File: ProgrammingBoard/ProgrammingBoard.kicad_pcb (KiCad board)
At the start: 4 copper layers, 34 x 69.5 mm, 6 parts, among them J1 X0511WVS-24AS-LPV01, J2 X0511FVS-24AS-LPV01, J3 X0511WVS-24AS-LPV01, J4 X0511FVS-24AS-LPV01, J5 Conn_01x20, J6 Conn_01x20

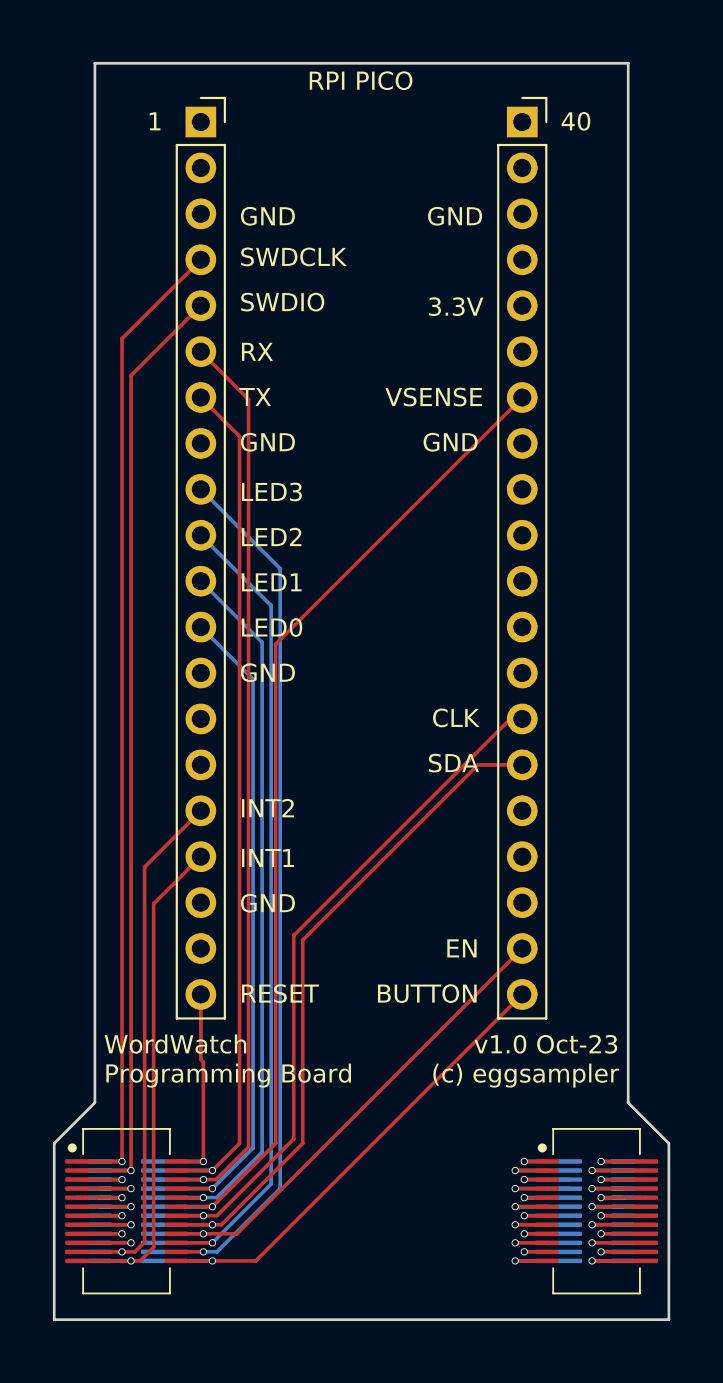
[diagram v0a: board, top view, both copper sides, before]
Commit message: Remove LED driver
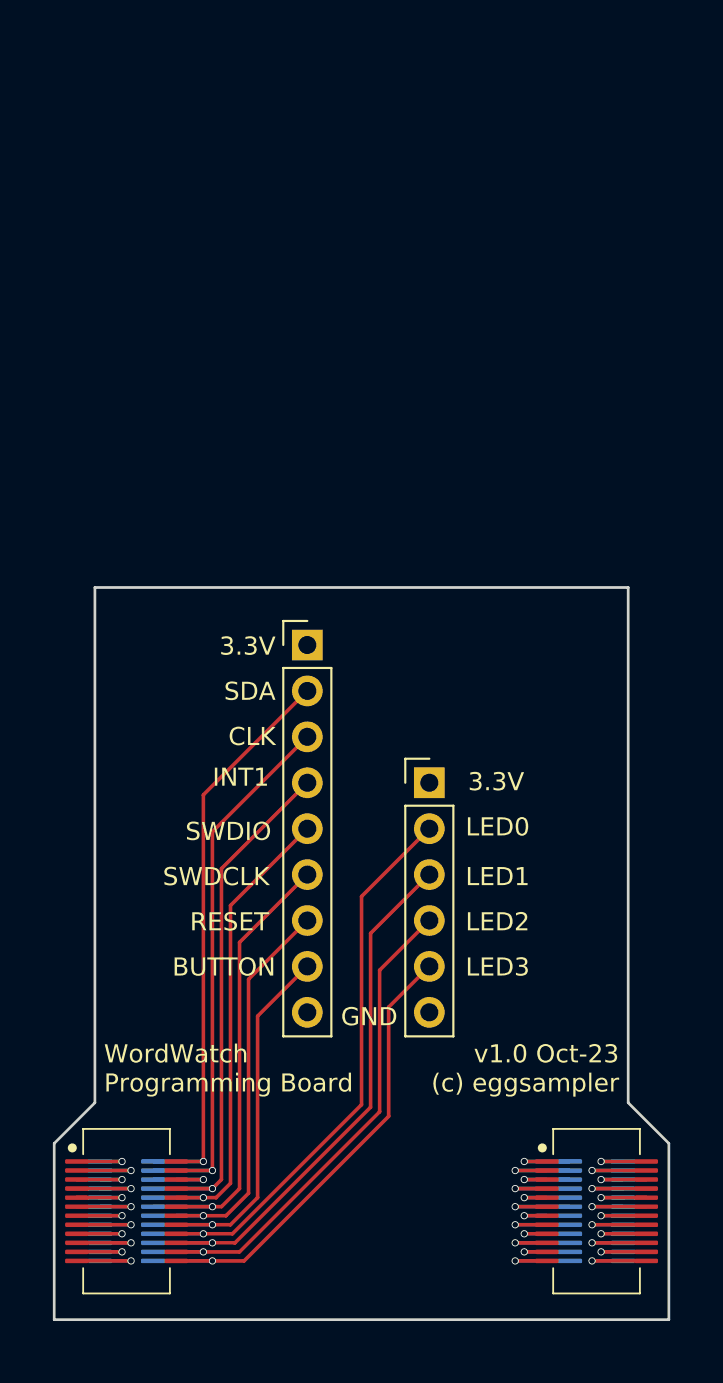
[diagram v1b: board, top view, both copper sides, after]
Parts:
- J5: value Conn_01x20 -> Conn_01x06; footprint Connector_PinSocket_2.54mm:PinSocket_1x20_P2.54mm_Vertical -> Connector_PinHeader_2.54mm:PinHeader_1x06_P2.54mm_Vertical
- J6: value Conn_01x20 -> Conn_01x09; footprint Connector_PinSocket_2.54mm:PinSocket_1x20_P2.54mm_Vertical -> Connector_PinHeader_2.54mm:PinHeader_1x09_P2.54mm_Vertical
- moved J5 38.7 mm to (130.8, 72.8)
- moved J6 31.3 mm to (124.0, 65.2)
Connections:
- J3 pad 1: /Connectors/RESET -> /Connectors/SDA
- J3 pad 11: /Connectors/VSENSE -> /Connectors/SWDCLK
- J3 pad 13: /Connectors/SCL -> /Connectors/RESET
- J3 pad 15: /Connectors/SDA -> /Connectors/BUTTON
- J3 pad 17: /Connectors/LED_EN -> /Connectors/LED0
- J3 pad 19: /Connectors/LED2 -> /Connectors/LED1
- J3 pad 2: /Connectors/SWDCLK -> VCC
- J3 pad 21: /Connectors/LED3 -> /Connectors/LED2
- J3 pad 22: /Connectors/INT2 -> GND
- J3 pad 23: /Connectors/BUTTON -> /Connectors/LED3
- J3 pad 24: /Connectors/INT1 -> GND
- J3 pad 3: /Connectors/TX -> /Connectors/SCL
- J3 pad 4: /Connectors/SWDIO -> VCC
- J3 pad 5: /Connectors/RX -> GND
- J3 pad 7: /Connectors/LED0 -> /Connectors/INT1
- J3 pad 9: /Connectors/LED1 -> /Connectors/SWDIO
- J4 pad 1: /Connectors/SWDCLK -> VCC
- J4 pad 10: /Connectors/LED1 -> /Connectors/SWDIO
- J4 pad 12: /Connectors/VSENSE -> /Connectors/SWDCLK
- J4 pad 14: /Connectors/SCL -> /Connectors/RESET
- J4 pad 16: /Connectors/SDA -> /Connectors/BUTTON
- J4 pad 18: /Connectors/LED_EN -> /Connectors/LED0
- J4 pad 2: /Connectors/RESET -> /Connectors/SDA
- J4 pad 20: /Connectors/LED2 -> /Connectors/LED1
- J4 pad 21: /Connectors/INT2 -> GND
- J4 pad 22: /Connectors/LED3 -> /Connectors/LED2
- J4 pad 23: /Connectors/INT1 -> GND
- J4 pad 24: /Connectors/BUTTON -> /Connectors/LED3
- J4 pad 3: /Connectors/SWDIO -> VCC
- J4 pad 4: /Connectors/TX -> /Connectors/SCL
- J4 pad 6: /Connectors/RX -> GND
- J4 pad 8: /Connectors/LED0 -> /Connectors/INT1
- J5 pad 1: unconnected-(J5-Pin_1-Pad1) -> VCC
- J5 pad 2: unconnected-(J5-Pin_2-Pad2) -> /Connectors/LED0
- J5 pad 3: GND -> /Connectors/LED1
- J5 pad 4: /Connectors/SWDCLK -> /Connectors/LED2
- J5 pad 5: /Connectors/SWDIO -> /Connectors/LED3
- J5 pad 6: /Connectors/RX -> GND
- J6 pad 1: unconnected-(J6-Pin_1-Pad1) -> VCC
- J6 pad 2: unconnected-(J6-Pin_2-Pad2) -> /Connectors/SDA
- J6 pad 3: GND -> /Connectors/SCL
- J6 pad 4: unconnected-(J6-Pin_4-Pad4) -> /Connectors/INT1
- J6 pad 5: VCC -> /Connectors/SWDIO
- J6 pad 6: unconnected-(J6-Pin_6-Pad6) -> /Connectors/SWDCLK
- J6 pad 7: /Connectors/VSENSE -> /Connectors/RESET
- J6 pad 8: GND -> /Connectors/BUTTON
- J6 pad 9: unconnected-(J6-Pin_9-Pad9) -> GND
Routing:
- net /Connectors/VSENSE: track 57.1 -> 0.00 mm, vias 1 -> 0
- net /Connectors/RX: track 52.6 -> 0.00 mm, vias 1 -> 0
- net /Connectors/TX: track 49.5 -> 0.00 mm, vias 1 -> 0
- net /Connectors/INT2: track 30.3 -> 0.00 mm, vias 1 -> 0
- net /Connectors/SWDCLK: track 55.4 -> 26.1 mm
- net /Connectors/LED_EN: track 28.5 -> 0.00 mm, vias 1 -> 0
- net /Connectors/SWDIO: track 54.2 -> 27.5 mm
- net /Connectors/LED3: track 50.5 -> 27.6 mm
- net /Connectors/LED2: track 47.4 -> 29.0 mm
- net GND: track 29.1 -> 41.8 mm, vias 7 -> 10
- net /Connectors/LED1: track 41.6 -> 31.3 mm
- net /Connectors/RESET: track 13.6 -> 23.7 mm
- net VCC: track 16.9 -> 25.3 mm, vias 4 -> 6
- net /Connectors/SCL: track 39.9 -> 31.4 mm
- net /Connectors/SDA: track 39.5 -> 32.7 mm
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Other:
- board size 34 x 69.5 mm -> 34 x 40.5 mm
- board text removed: "1"
- board text removed: "40"
- board text removed: "EN"
- board text removed: "INT2"
- board text removed: "RPI PICO"
- board text removed: "RX"
- board text removed: "TX"
- board text removed: "VSENSE"

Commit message: Change led matrix routing for sinking current through mcu, sourcing from battery
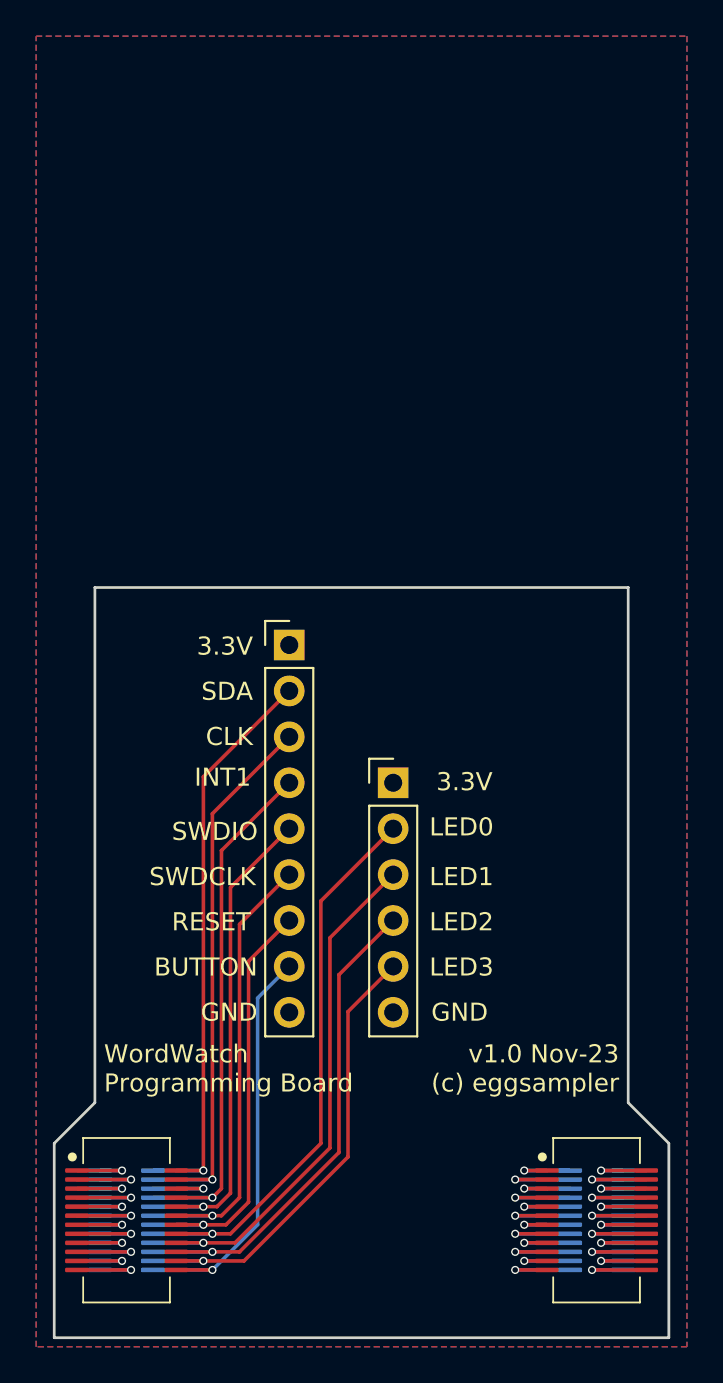
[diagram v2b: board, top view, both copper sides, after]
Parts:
- moved J5 2.00 mm to (128.8, 72.8)
- moved J6 1.00 mm to (123.0, 65.2)
- moved J1 0.50 mm to (140.0, 97.0)
- moved J2 0.50 mm to (140.0, 97.0)
- moved J3 0.50 mm to (114.0, 97.0)
- moved J4 0.50 mm to (114.0, 97.0)
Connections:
- J1 pad 10: /Connectors/COL1 -> /Connectors/ROW3
- J1 pad 11: /Connectors/ROW4 -> /Connectors/COL4
- J1 pad 12: /Connectors/COL2 -> /Connectors/ROW4
- J1 pad 13: /Connectors/ROW5 -> /Connectors/COL5
- J1 pad 14: /Connectors/COL3 -> /Connectors/ROW5
- J1 pad 15: /Connectors/ROW6 -> /Connectors/COL6
- J1 pad 16: /Connectors/COL4 -> /Connectors/ROW6
- J1 pad 17: /Connectors/ROW7 -> /Connectors/COL7
- J1 pad 18: /Connectors/COL5 -> /Connectors/ROW7
- J1 pad 19: /Connectors/ROW8 -> /Connectors/COL8
- J1 pad 20: /Connectors/COL6 -> /Connectors/ROW8
- J1 pad 21: /Connectors/ROW9 -> /Connectors/COL9
- J1 pad 22: /Connectors/COL7 -> /Connectors/ROW9
- J1 pad 23: GND -> /Connectors/COL10
- J1 pad 24: /Connectors/COL8 -> GND
- J1 pad 3: /Connectors/ROW0 -> /Connectors/COL0
- J1 pad 4: /Connectors/COL9 -> /Connectors/ROW0
- J1 pad 5: /Connectors/ROW1 -> /Connectors/COL1
- J1 pad 6: /Connectors/COL10 -> /Connectors/ROW1
- J1 pad 7: /Connectors/ROW2 -> /Connectors/COL2
- J1 pad 8: /Connectors/COL0 -> /Connectors/ROW2
- J1 pad 9: /Connectors/ROW3 -> /Connectors/COL3
- J2 pad 10: /Connectors/ROW3 -> /Connectors/COL3
- J2 pad 11: /Connectors/COL2 -> /Connectors/ROW4
- J2 pad 12: /Connectors/ROW4 -> /Connectors/COL4
- J2 pad 13: /Connectors/COL3 -> /Connectors/ROW5
- J2 pad 14: /Connectors/ROW5 -> /Connectors/COL5
- J2 pad 15: /Connectors/COL4 -> /Connectors/ROW6
- J2 pad 16: /Connectors/ROW6 -> /Connectors/COL6
- J2 pad 17: /Connectors/COL5 -> /Connectors/ROW7
- J2 pad 18: /Connectors/ROW7 -> /Connectors/COL7
- J2 pad 19: /Connectors/COL6 -> /Connectors/ROW8
- J2 pad 20: /Connectors/ROW8 -> /Connectors/COL8
- J2 pad 21: /Connectors/COL7 -> /Connectors/ROW9
- J2 pad 22: /Connectors/ROW9 -> /Connectors/COL9
- J2 pad 23: /Connectors/COL8 -> GND
- J2 pad 24: GND -> /Connectors/COL10
- J2 pad 3: /Connectors/COL9 -> /Connectors/ROW0
- J2 pad 4: /Connectors/ROW0 -> /Connectors/COL0
- J2 pad 5: /Connectors/COL10 -> /Connectors/ROW1
- J2 pad 6: /Connectors/ROW1 -> /Connectors/COL1
- J2 pad 7: /Connectors/COL0 -> /Connectors/ROW2
- J2 pad 8: /Connectors/ROW2 -> /Connectors/COL2
- J2 pad 9: /Connectors/COL1 -> /Connectors/ROW3
- J3 pad 15: /Connectors/BUTTON -> /Connectors/LED0
- J3 pad 17: /Connectors/LED0 -> /Connectors/LED1
- J3 pad 19: /Connectors/LED1 -> /Connectors/LED2
- J3 pad 21: /Connectors/LED2 -> /Connectors/LED3
- J3 pad 23: /Connectors/LED3 -> /Connectors/BUTTON
- J4 pad 16: /Connectors/BUTTON -> /Connectors/LED0
- J4 pad 18: /Connectors/LED0 -> /Connectors/LED1
- J4 pad 20: /Connectors/LED1 -> /Connectors/LED2
- J4 pad 22: /Connectors/LED2 -> /Connectors/LED3
- J4 pad 24: /Connectors/LED3 -> /Connectors/BUTTON
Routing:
- net /Connectors/BUTTON: track 22.3 -> 23.8 mm
- net /Connectors/LED1: track 31.3 -> 30.0 mm
- net /Connectors/LED3: track 27.6 -> 26.2 mm
- net /Connectors/COL9: track 4.78 -> 3.72 mm
- net /Connectors/COL10: track 3.78 -> 4.72 mm
- added copper zone on B.Cu, net GND
- added copper zone on F.Cu, net GND
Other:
- board size 34 x 40.5 mm -> 34 x 41.5 mm
- board text added: "v1.0 Nov-23 (c) eggsampler"
- board text removed: "v1.0 Oct-23 (c) eggsampler"
